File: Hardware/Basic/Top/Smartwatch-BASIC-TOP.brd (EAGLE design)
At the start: 38 x 38 mm, 52 parts, among them U2 NRF52832_MODULE_MDBT42, U4 CP2104

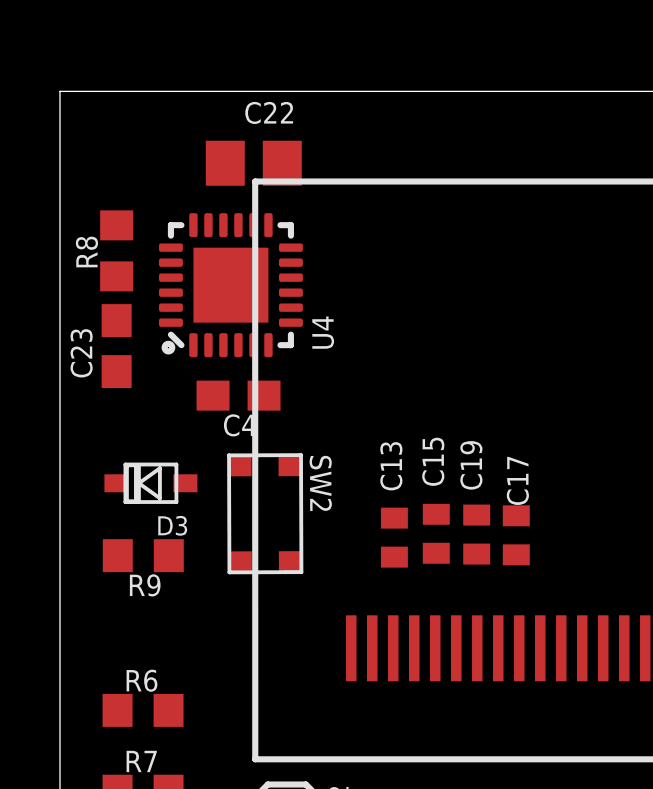
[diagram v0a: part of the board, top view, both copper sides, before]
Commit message: USB, OLED Microcontroller and SD added. Need to add RTC
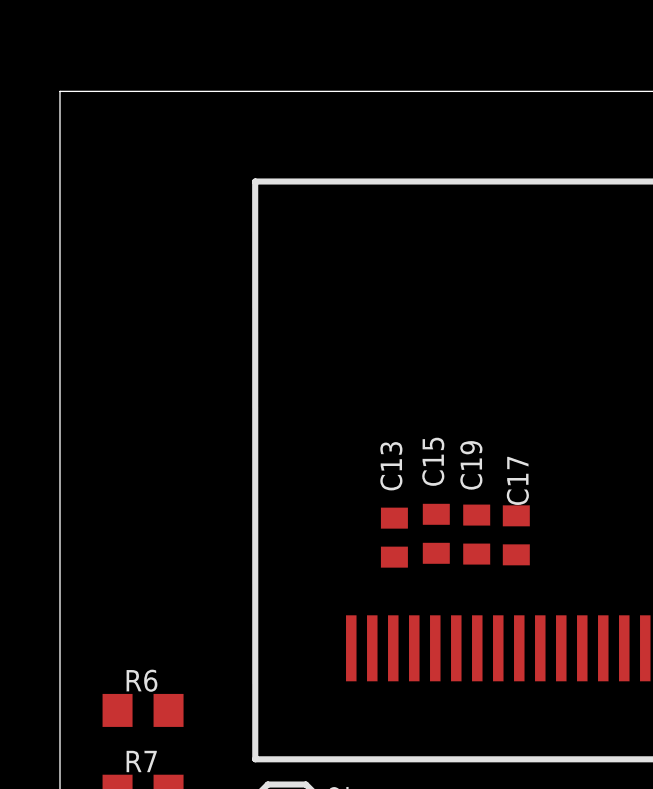
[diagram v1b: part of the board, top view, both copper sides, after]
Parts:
- removed C22: 10u, LinnesLab-Passives:C0805
- removed C23, C4: 100n, LinnesLab-Passives:C0603
- removed D3: (no value), LinnesLab-DiscreteSemi:USC
- removed R8: 1k, LinnesLab-Passives:R0603
- removed R9: 10k, LinnesLab-Passives:R0603
- removed SW2: (no value), LinnesLab-Switches:BUTTON-GULLWING
- removed U4: CP2104, LinnesLab-DigitalIC:QFN24_4MM_SMSC
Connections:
- removed net N$19: R8.1, U4.21
- removed net N$20: C22.2, U4.16
- removed net USB.D+: U4.3
- removed net USB.D-: U4.4
- removed net VCCIO: C4.1, U4.5, U4.6
- net 3.3V: no longer D3.-, R9.2
- net DTR: no longer C23.1, U4.23
- net GND: no longer C22.1, C4.2, SW2.3, U4.2, U4.THERM
- net N$1: no longer U4.8
- net RESET: no longer C23.2, D3.+, R9.1, SW2.1
- net RXD: no longer R8.2
- net TXD: no longer U4.20
- net V_USB: no longer U4.7

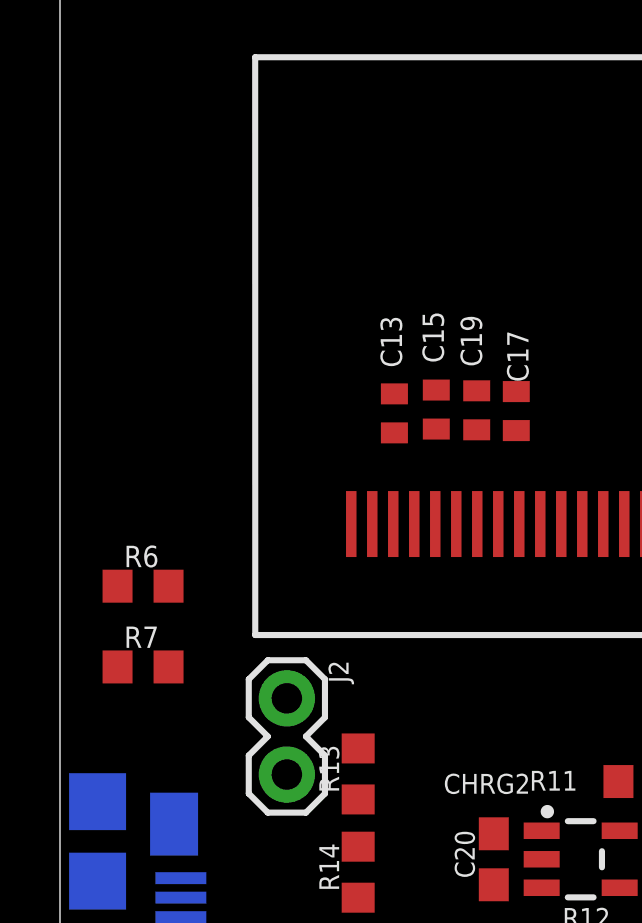
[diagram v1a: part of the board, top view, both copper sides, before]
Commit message: USB, OLED Microcontroller, SD and RTC added
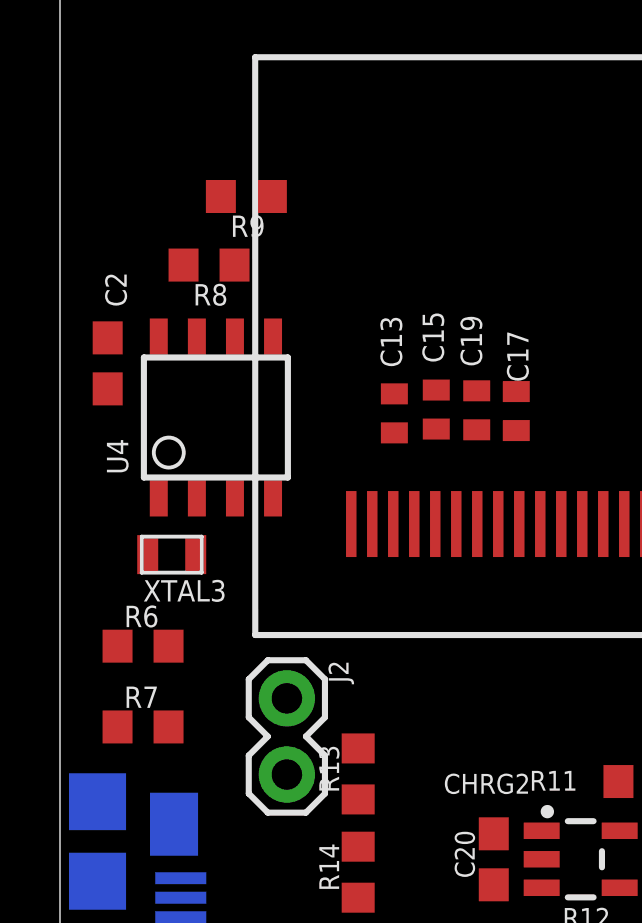
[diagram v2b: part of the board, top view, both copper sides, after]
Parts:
- added C2: 1u, LinnesLab-Passives:C0603
- added R8, R9: 10k, LinnesLab-Passives:R0603
- added U4: PCF8523, LinnesLab-Clocks:SO8
- added XTAL3: 32.7680kHz, LinnesLab-Clocks:2-SMD.NOLEAD.2.0MMTO1.2MM
- moved R7 2.00 mm to (2.77, 12.7)
- moved R6 2.00 mm to (2.77, 15.4)
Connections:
- new net N$19: U4.2, XTAL3.P$1
- new net N$20: U4.1, XTAL3.P$2
- new net VBATT: U4.3
- net 3.3V: now also C2.1, R8.2, R9.2, U4.8
- net GND: now also C2.2, U4.4
- net SCL: now also R8.1, U4.6
- net SDA: now also R9.1, U4.5

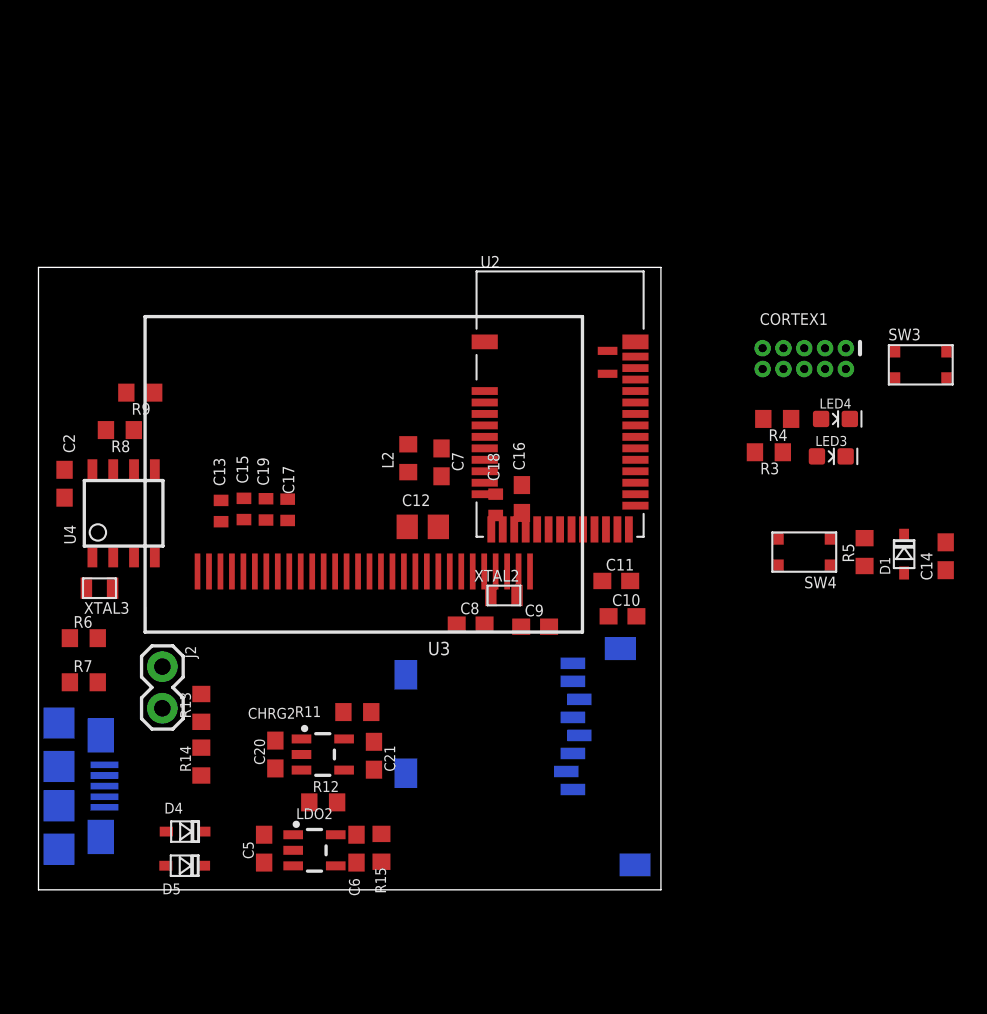
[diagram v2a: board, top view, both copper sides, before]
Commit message: Added FTDI
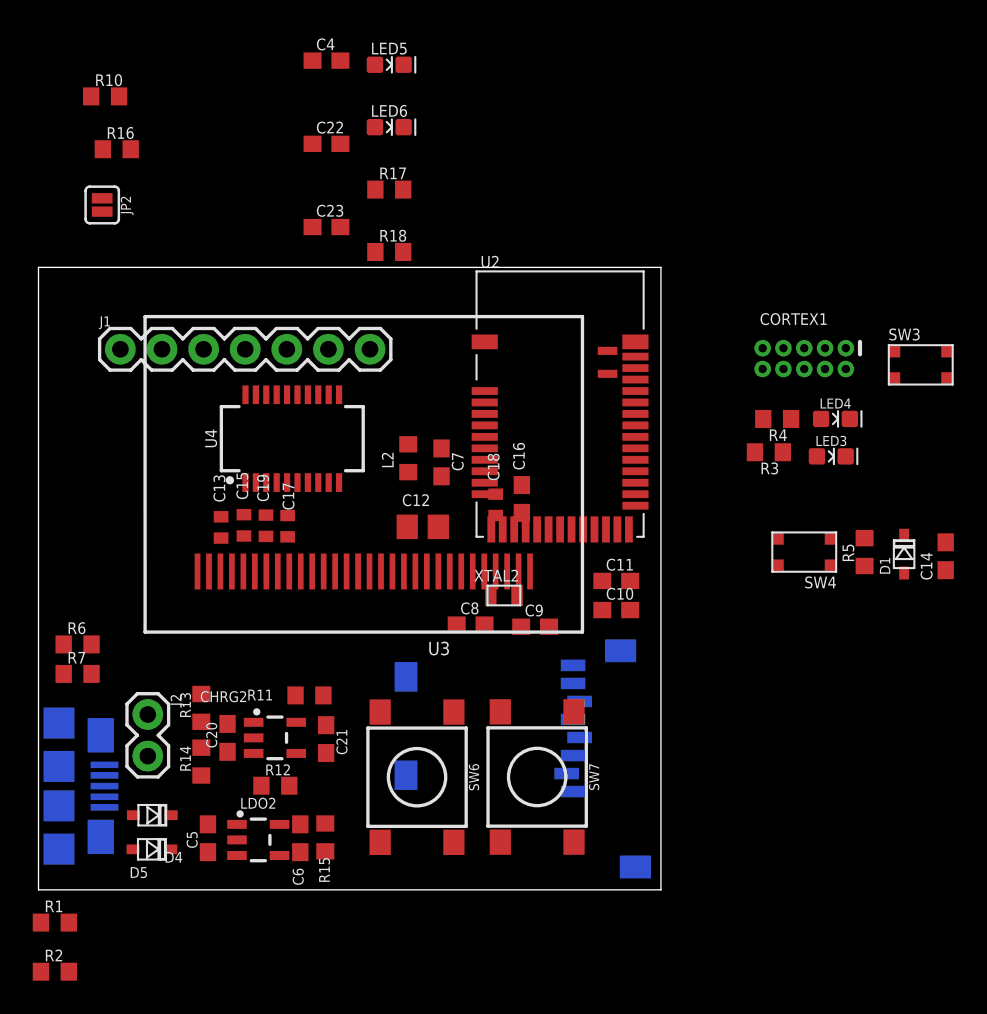
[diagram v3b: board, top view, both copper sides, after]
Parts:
- removed C2: 1u, LinnesLab-Passives:C0603
- removed R8, R9: 10k, LinnesLab-Passives:R0603
- removed XTAL3: 32.7680kHz, LinnesLab-Clocks:2-SMD.NOLEAD.2.0MMTO1.2MM
- added C22, C23: 47p, LinnesLab-Passives:C0603
- added C4: 100n, LinnesLab-Passives:C0603
- added J1: (no value), LinnesLab-Connectors:1X07
- added JP2: (no value), LinnesLab-Switches:SMT-JUMPER_2_NO_SILK
- added LED5: RED, LinnesLab-LED:LED-0603
- added LED6: YELLOW, LinnesLab-LED:LED-0603
- added R1, R2: 10k, LinnesLab-Passives:R0603
- added R10, R16: 27, LinnesLab-Passives:R0603
- added R17, R18: 1k, LinnesLab-Passives:R0603
- added SW6, SW7: SWITCH.MOM, LinnesLab-Switches:TACTILE_SWITCH_SMD_6.2MM_TALL
- U4: value PCF8523 -> FT231XS; device LinnesLab-Clocks:SO8 -> LinnesLab-DigitalIC:SSOP20_L
- moved U4 11.3 mm to (15.5, 27.5), turned to 0 degrees
- moved LDO2 3.49 mm to (13.4, 3.05)
- moved C5 3.49 mm to (10.3, 3.15)
- moved C6 3.49 mm to (16.0, 3.15)
- moved R15 3.49 mm to (17.5, 3.20)
- moved C20 3.09 mm to (11.5, 9.28)
- moved CHRG2 3.09 mm to (14.4, 9.28)
- moved C21 3.09 mm to (17.6, 9.20)
- moved R11 3.09 mm to (16.5, 11.9)
- moved R12 3.09 mm to (14.5, 6.36)
- moved J2 3.05 mm to (6.67, 10.7)
- moved D4 2.24 mm to (6.95, 4.56)
- moved D5 2.24 mm to (6.92, 2.47)
- moved C13 1.00 mm to (11.1, 22.1)
- moved C15 1.00 mm to (12.5, 22.3)
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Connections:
- removed net BATT: R13.1, R14.2
- removed net CD1: SD2.CD1
- removed net CHRG.STAT: CHRG2.1, R12.1
- removed net N$19: U4.2, XTAL3.P$1
- removed net N$20: U4.1, XTAL3.P$2
- removed net SD.CS: SD2.2
- removed net VBATT: U4.3
- new net !CTS: JP2.2, U4.9
- new net !DTR: U4.1
- new net A4/BATT: R13.1, R14.2, U2.5
- new net D27/CHRG.STAT: CHRG2.1, R12.1, U2.4
- new net D5/CD1: SD2.CD1, U2.18
- new net D7/SD.CS: SD2.2, U2.20
- new net FT3V3: U4.13
- new net N$21: SW7.B1, SW7.B2
- new net N$22: SW6.B1, SW6.B2
- new net N$23: SW6.A1
- new net N$24: SW7.A1
- new net N$25: R10.2, U4.12
- new net N$26: R16.2, U4.11
- new net N$27: LED5.C, R17.2
- new net N$28: LED6.C, R18.2
- new net RXLED: R17.1, U4.17
- new net TXLED: R18.1, U4.10
- net 3.3V: now also C4.2, LED5.A, LED6.A, R1.2, R2.2, U4.14, U4.3; no longer C2.1, R8.2, R9.2, U4.8
- net GND: now also C22.2, C23.1, C4.1, JP2.1, U4.16, U4.6; no longer C2.2, U4.4
- net RXD: now also U4.4
- net SCL: now also R2.1; no longer R8.1, U4.6
- net SDA: now also R1.1; no longer R9.1, U4.5
- net TXD: now also U4.20
- net USB+: now also C22.1, R16.1
- net USB-: now also C23.2, R10.1
- net V_USB: now also U4.15

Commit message: Bottom board routed
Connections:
- removed net CS.OLED: U3.13
- removed net DC.OLED: U3.15
- removed net N$23: SW6.A1
- removed net N$24: SW7.A1
- removed net RESET.OLED: U3.14
- new net A6/TIA: U2.7
- new net A7/PPG: U2.8
- new net D11/SW1: SW7.A1, U2.25
- new net D15/SW2: SW6.A1, U2.29
- new net D16/CS.OLED: U2.30, U3.13
- new net D29/LED.CTRL: U2.6
- new net D3/RESET.OLED: U2.16, U3.14
- new net D4/DC.OLED: U2.17, U3.15
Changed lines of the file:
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@@
 <contactref element="U2" pad="38"/>
 </signal>
-<signal name="DC.OLED">
+<signal name="D4/DC.OLED">
 <contactref element="U3" pad="15"/>
-</signal>
-<signal name="RESET.OLED">
-<contactref element="U3" pad="14"/>
+<contactref element="U2" pad="17"/>
+<wire x1="19.509" y1="19.436" x2="31.143" y2="22.003" width="0" layer="19" extent="1-1"/>
 </signal>
 <signal name="N$1">
@@
 <wire x1="27.909" y1="19.436" x2="27.9108" y2="24.1562" width="0" layer="19" extent="1-1"/>
 </signal>
-<signal name="CS.OLED">
+<signal name="D16/CS.OLED">
 <contactref element="U3" pad="13"/>
+<contactref element="U2" pad="30"/>
+<wire x1="18.109" y1="19.436" x2="36.443" y2="26.953" width="0" layer="19" extent="1-1"/>
 </signal>
 <signal name="N$17">
@@
 <wire x1="25.36" y1="10.851" x2="25.36" y2="2.901" width="0" layer="19" extent="1-1"/>
 </signal>
-<signal name="N$23">
-<contactref element="SW6" pad="A1"/>
-</signal>
-<signal name="N$24">
-<contactref element="SW7" pad="A1"/>
-</signal>
 <signal name="CD2">
 <contactref element="SD2" pad="CD2"/>
@@
 <wire x1="22.44" y1="13" x2="31.843" y2="22.003" width="0" layer="19" extent="1-16"/>
 </signal>
+<signal name="D11/SW1">
+<contactref element="U2" pad="25"/>
+<contactref element="SW7" pad="A1"/>
+<wire x1="28.194" y1="10.864" x2="36.443" y2="23.453" width="0" layer="19" extent="1-1"/>
+</signal>
+<signal name="D15/SW2">
+<contactref element="U2" pad="29"/>
+<contactref element="SW6" pad="A1"/>
+<wire x1="20.86" y1="10.851" x2="36.443" y2="26.253" width="0" layer="19" extent="1-1"/>
+</signal>
+<signal name="D3/RESET.OLED">
+<contactref element="U2" pad="16"/>
+<contactref element="U3" pad="14"/>
+<wire x1="18.809" y1="19.436" x2="30.443" y2="22.003" width="0" layer="19" extent="1-1"/>
+</signal>
+<signal name="D29/LED.CTRL">
+<contactref element="U2" pad="6"/>
+</signal>
+<signal name="A6/TIA">
+<contactref element="U2" pad="7"/>
+</signal>
+<signal name="A7/PPG">
+<contactref element="U2" pad="8"/>
+</signal>
 </signals>

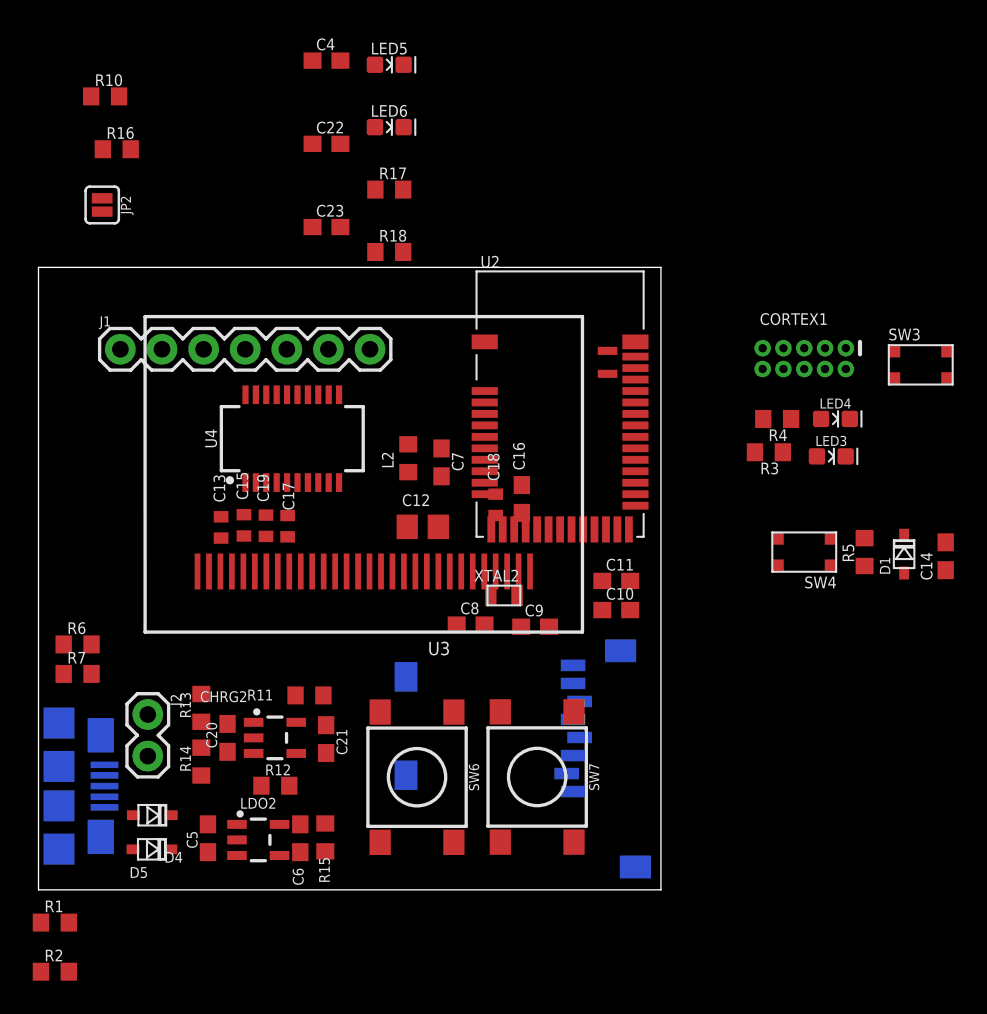
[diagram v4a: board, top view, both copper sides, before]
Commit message: Top board routing started
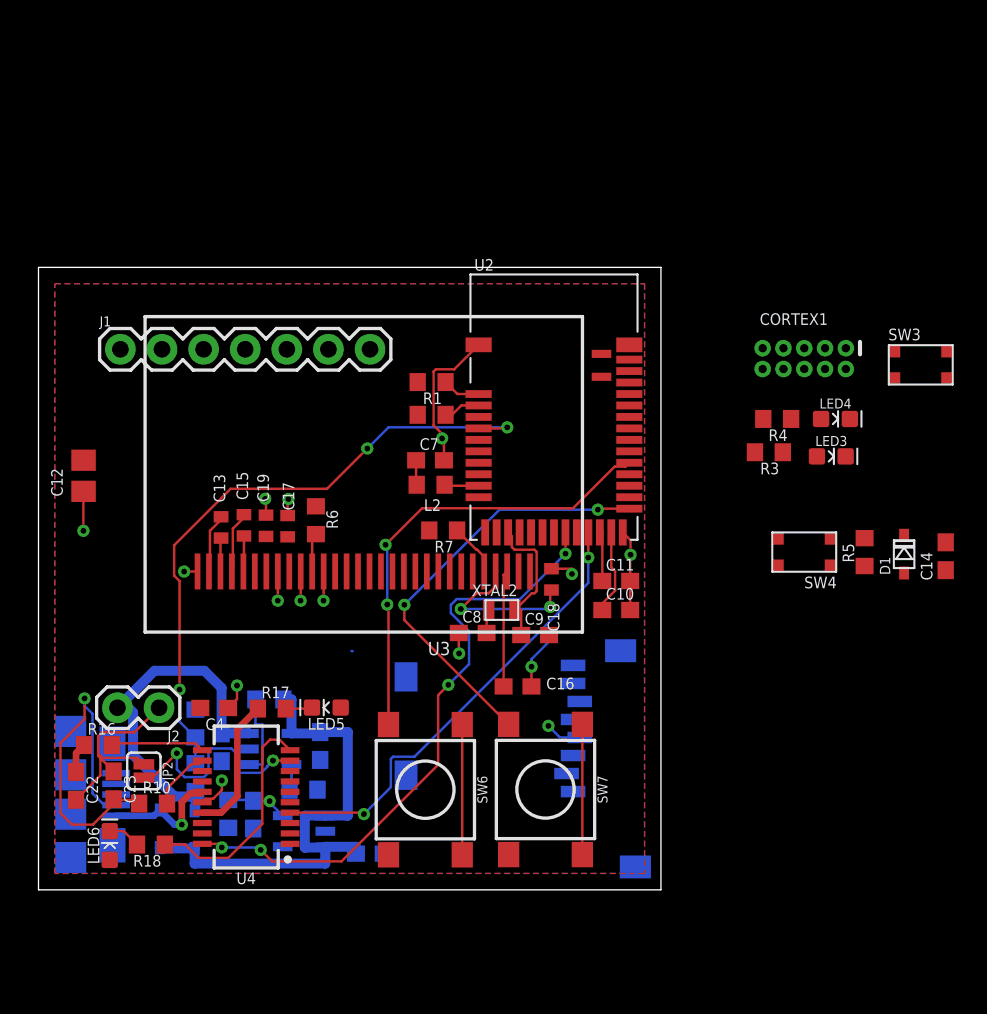
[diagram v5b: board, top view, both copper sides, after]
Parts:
- moved LED6 47.1 mm to (4.35, 2.70), turned to 90 degrees
- moved R10 43.3 mm to (7.00, 5.26)
- moved C22 42.1 mm to (2.29, 6.35), turned to 270 degrees
- moved R2 41.0 mm to (24.0, 29.0), turned to 180 degrees
- moved R1 40.2 mm to (24.0, 31.0), turned to 180 degrees
- moved C4 40.1 mm to (10.7, 11.1), turned to 180 degrees
- moved LED5 39.4 mm to (17.6, 11.1), turned to 180 degrees
- moved R18 39.0 mm to (6.87, 2.77), turned to 180 degrees
- moved C23 36.5 mm to (4.58, 6.38), turned to 270 degrees
- moved R16 36.4 mm to (3.63, 8.84)
- moved JP2 34.6 mm to (6.43, 7.26)
- moved R17 32.5 mm to (14.2, 11.1)
- moved R7 24.0 mm to (24.7, 21.9), turned to 180 degrees
- moved U4 22.1 mm to (12.7, 5.66), turned to 90 degrees
- moved C12 20.9 mm to (2.75, 25.3), turned to 90 degrees
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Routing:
- net GND: track 0.00 -> 48.3 mm, vias 0 -> 14
- net A4/BATT: track 0.00 -> 38.9 mm, vias 0 -> 3
- net TXD: track 0.00 -> 37.9 mm, vias 0 -> 4
- net VIN: track 0.00 -> 31.9 mm
- net RXD: track 0.00 -> 28.2 mm, vias 0 -> 2
- net D15/SW2: track 0.00 -> 28.0 mm, vias 0 -> 2
- net D11/SW1: track 0.00 -> 26.1 mm, vias 0 -> 2
- net VLIPO: track 0.00 -> 22.2 mm
- net USB-: track 0.00 -> 21.7 mm, vias 0 -> 1
- net !CTS: track 0.00 -> 14.4 mm, vias 0 -> 2
- net TXLED: track 0.00 -> 14.0 mm
- net N$15: track 0.00 -> 10.3 mm, vias 0 -> 2
- net N$6: track 0.00 -> 8.73 mm
- net RXLED: track 0.00 -> 8.43 mm
- net N$22: track 0.00 -> 7.95 mm
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- added copper zone on layer 1, net 3.3V
- added copper zone on layer 16, net GND
